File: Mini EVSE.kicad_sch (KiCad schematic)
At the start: 39 parts, among them IC1 ATtiny84-20P, IC2 UCC23511QDWYRQ1, IC3 TLP3547_TP1,F_O, J1 ICP, SW1 SW_DIP_x01, X1 15.36MHz

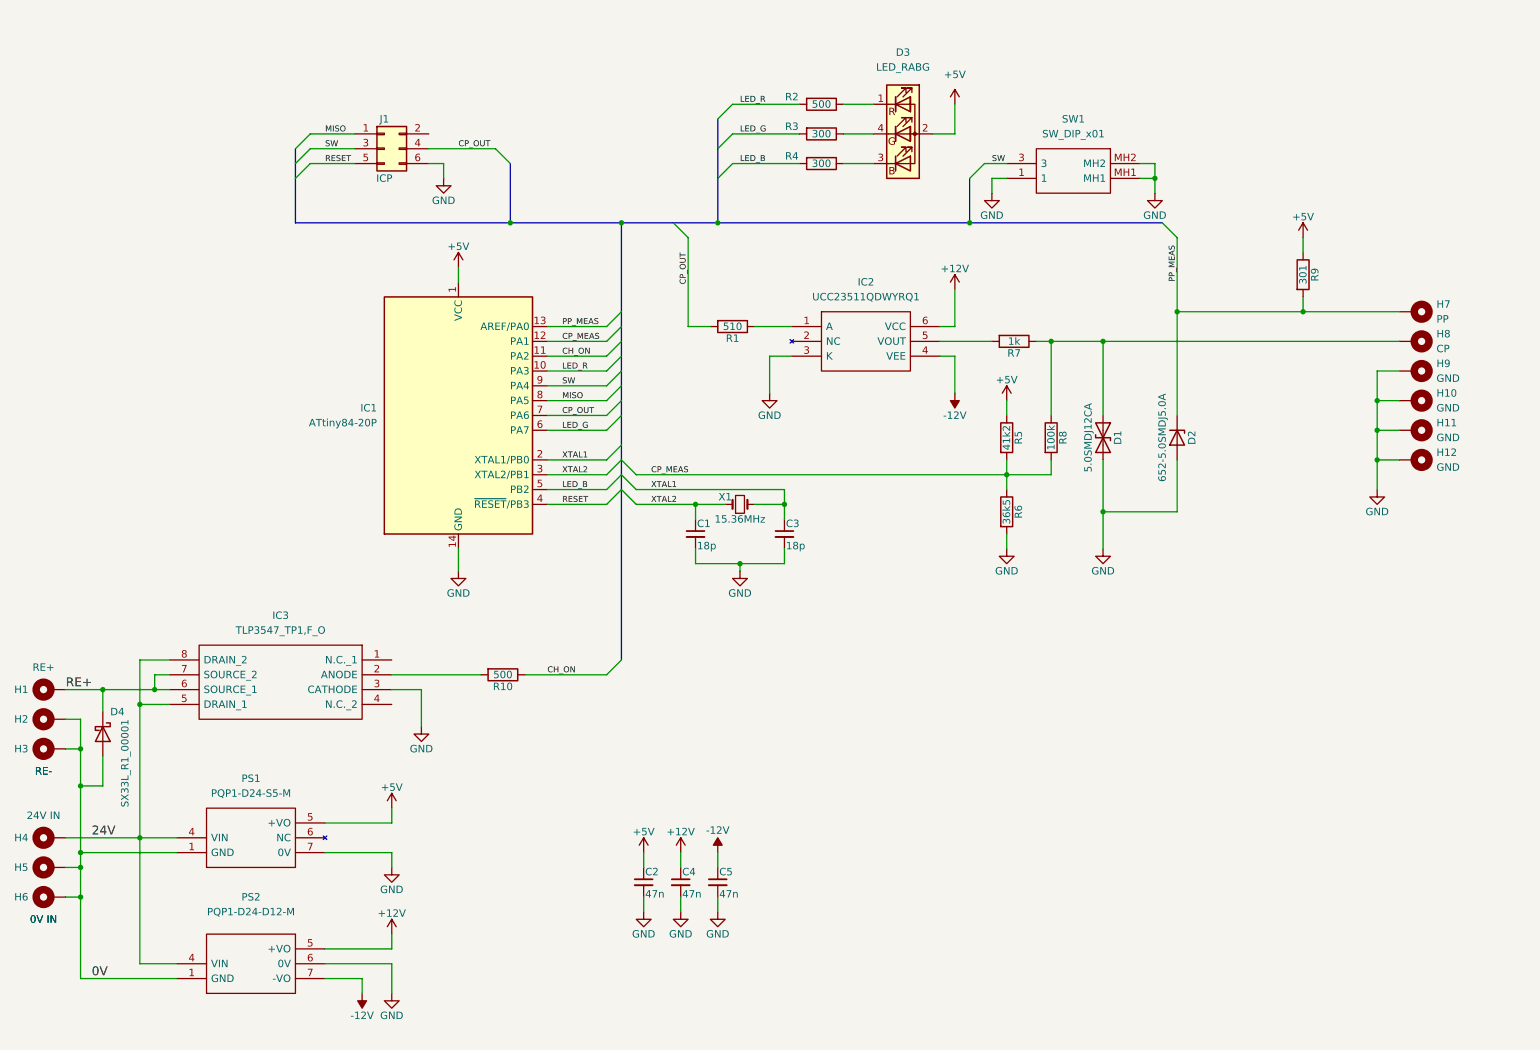
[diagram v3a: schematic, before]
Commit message: Working on better EMC immunity
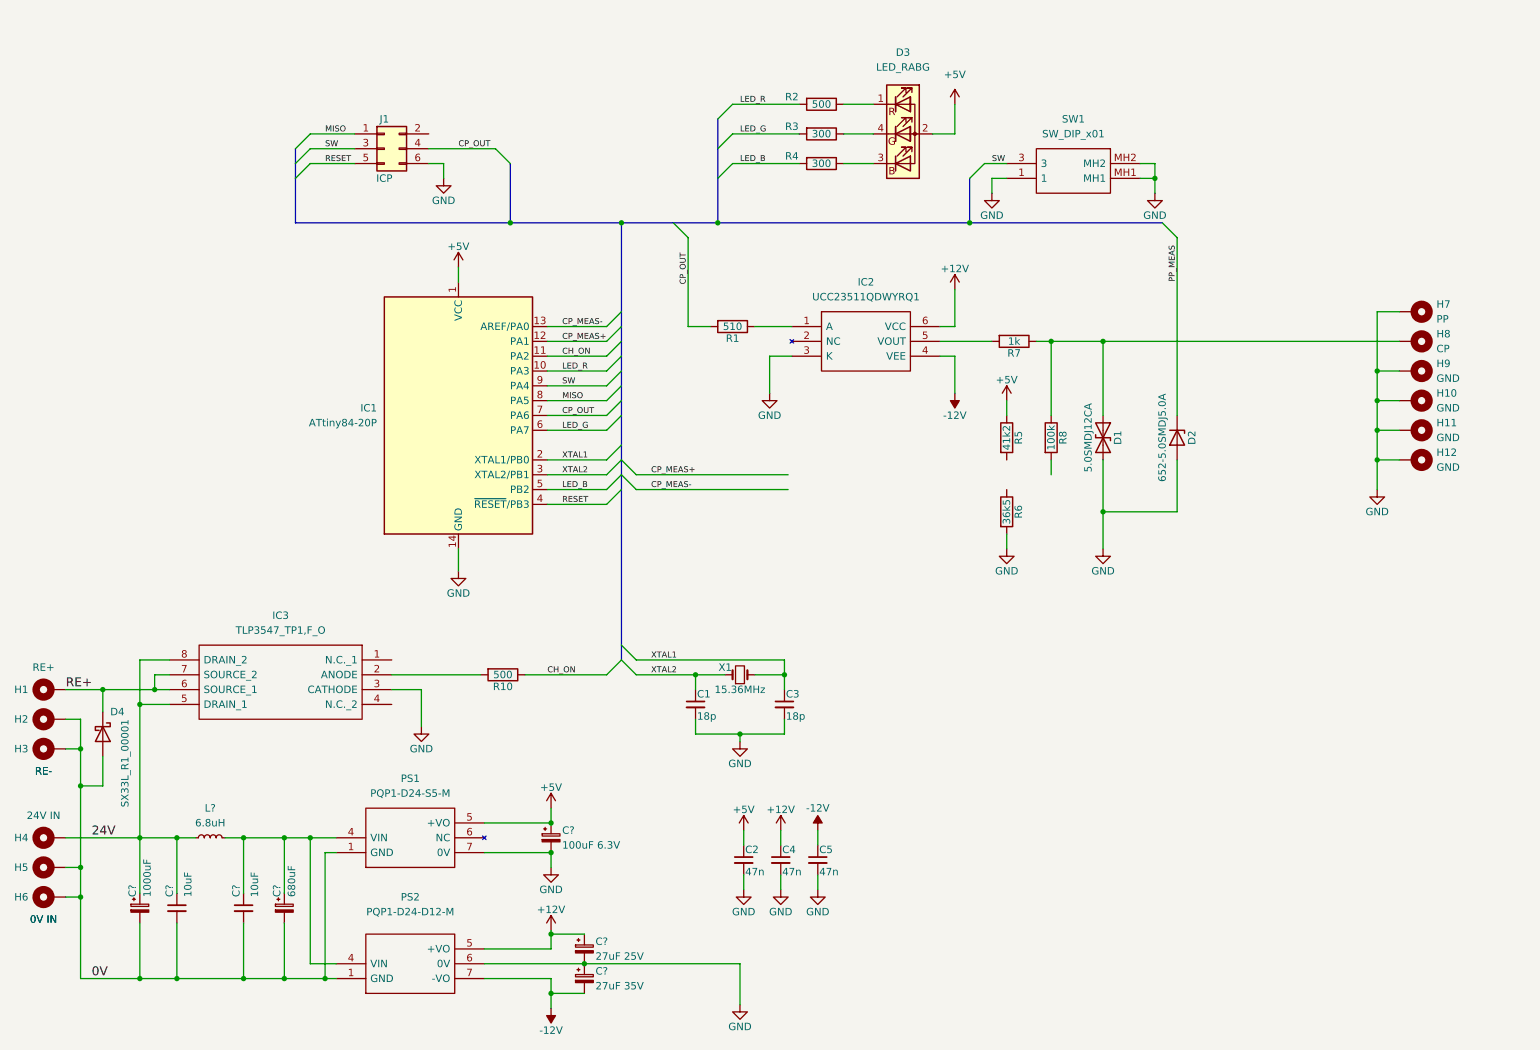
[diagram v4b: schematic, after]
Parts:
- removed R9: 301, Resistor_SMD:R_1210_3225Metric_Pad1.30x2.65mm_HandSolder, symbol Device:R
- added C? (x2): 10uF, symbol Device:C_Small
- added C?: 27uF 25V, symbol Device:C_Polarized_Small
- added C?: 1000uF, symbol Device:C_Polarized_Small
- added C?: 27uF 35V, symbol Device:C_Polarized_Small
- added C?: 100uF 6.3V, symbol Device:C_Polarized_Small
- added C?: 680uF, symbol Device:C_Polarized_Small
- added L?: 6.8uH, symbol Device:L_Small
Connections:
- net +12V: now also C?.1
- net +5V: now also C?.1
- net -12V: now also C?.2
- net 0V: now also C?.2, C?.2, C?.2, C?.2
- net 24V: now also C?.1, C?.1, L?.1; no longer PS1.4 (VIN), PS2.4 (VIN)
- net GND: now also H7.1, C?.1, C?.2, C?.2
- net PP_MEAS: no longer H7.1, IC1.13 (AREF/PA0)
- removed net CP_MEAS: IC1.12 (PA1), R5.2, R6.1, R8.2
- new net: C?.1, C?.1, L?.2, PS1.4 (VIN), PS2.4 (VIN)
- new net CP_MEAS+: IC1.12 (PA1)
- new net CP_MEAS-: IC1.13 (AREF/PA0)
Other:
- moved on the sheet: C1, C2, C3, C4, C5, PS1, PS2, X1

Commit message: Better EMC protection
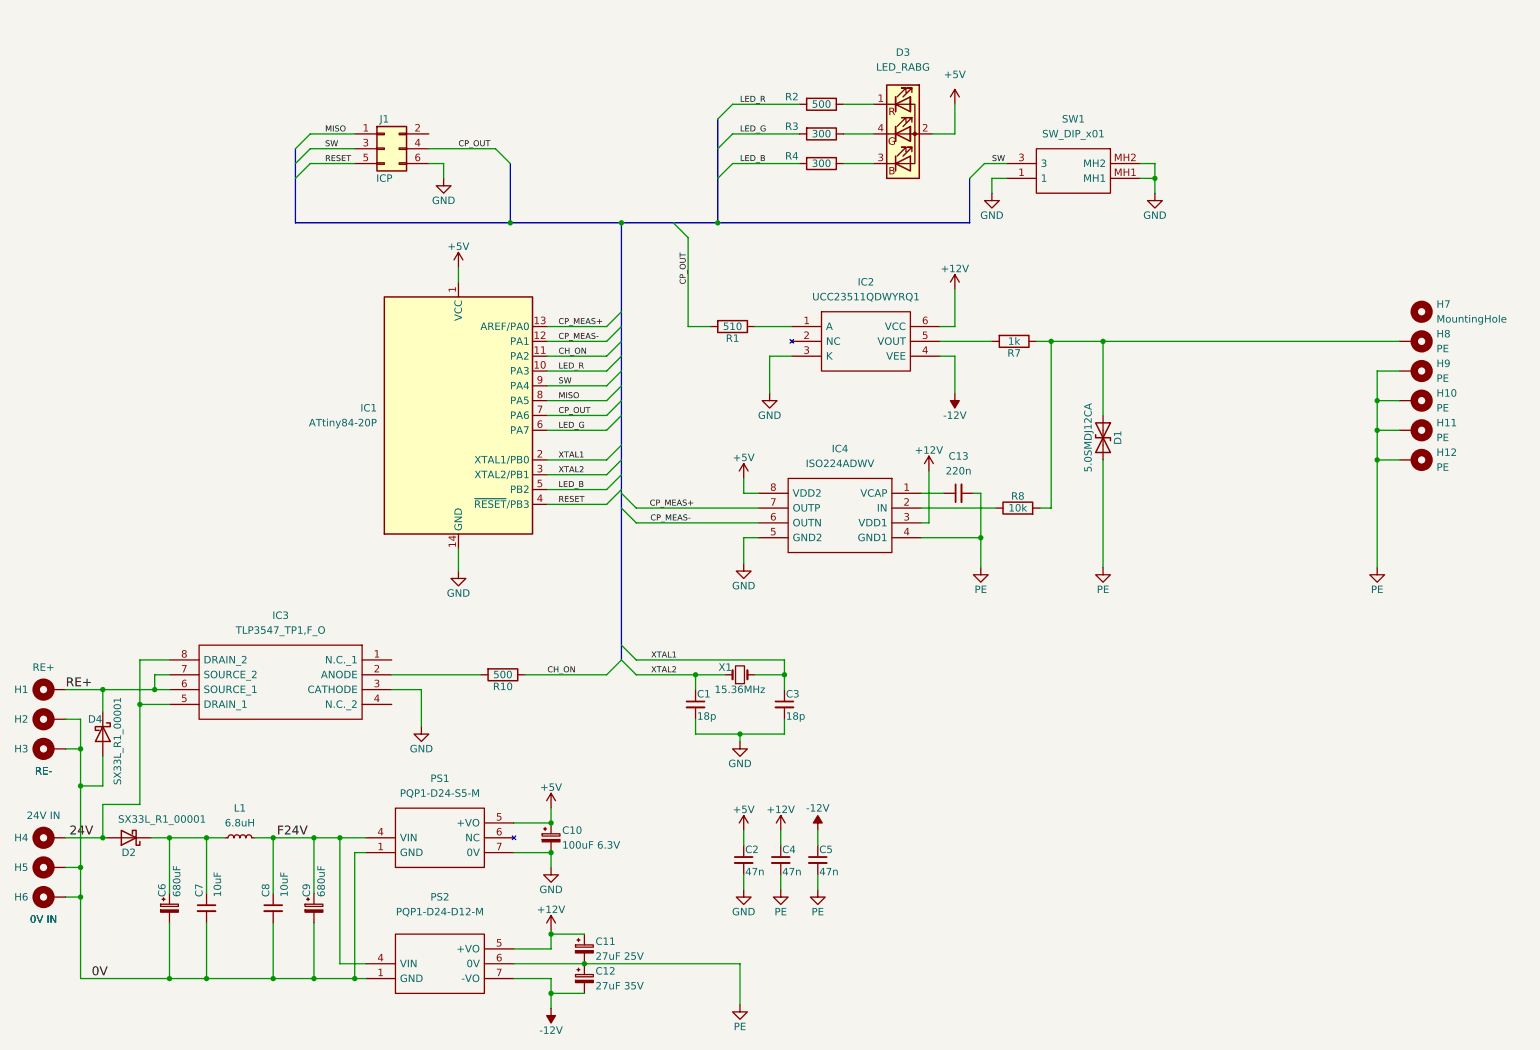
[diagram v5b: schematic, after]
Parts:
- removed D2: 652-5.0SMDJ5.0A, Diode_SMD:D_SMC, symbol Device:D_Zener
- removed H7: PP, TestPoint:TestPoint_Loop_D2.60mm_Drill1.4mm_Beaded, symbol Mechanical:MountingHole_Pad
- removed R5: 41k2, Resistor_SMD:R_1210_3225Metric_Pad1.30x2.65mm_HandSolder, symbol Device:R
- removed R6: 36k5, Resistor_SMD:R_1210_3225Metric_Pad1.30x2.65mm_HandSolder, symbol Device:R
- added C13: 220n, Capacitor_SMD:C_1206_3216Metric_Pad1.33x1.80mm_HandSolder, symbol Device:C_Small
- added D2: SX33L_R1_00001, Diode_SMD:D_SMA_Handsoldering, symbol Device:D_Schottky
- added H7: MountingHole, MountingHole:MountingHole_2.1mm, symbol Mechanical:MountingHole
- added IC4: ISO224ADWV, SamacSys_Parts:SOIC127P1150X280-8N, symbol SamacSys_Parts:ISO224ADWV
- C10: renamed from C?; footprint (none) -> Capacitor_SMD:CP_Elec_6.3x5.9
- C11, C12: renamed from C?; footprint (none) -> Capacitor_SMD:CP_Elec_5x5.8
- C6: renamed from C?; value 1000uF -> 680uF; footprint (none) -> Capacitor_SMD:CP_Elec_10x10.5
- C7, C8: renamed from C?; footprint (none) -> Capacitor_SMD:C_1206_3216Metric_Pad1.33x1.80mm_HandSolder
- C9: renamed from C?; footprint (none) -> Capacitor_SMD:CP_Elec_10x10.5
- H10, H11, H12, H9: value GND -> PE
- H8: value CP -> PE
- L1: renamed from L?; footprint (none) -> Inductor_SMD:L_1210_3225Metric_Pad1.42x2.65mm_HandSolder
- R1, R10, R2, R3, R4, R7: footprint Resistor_SMD:R_1210_3225Metric_Pad1.30x2.65mm_HandSolder -> Resistor_SMD:R_1206_3216Metric_Pad1.30x1.75mm_HandSolder
- R8: value 100k -> 10k; footprint Resistor_SMD:R_1210_3225Metric_Pad1.30x2.65mm_HandSolder -> Resistor_SMD:R_1206_3216Metric_Pad1.30x1.75mm_HandSolder
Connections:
- net +12V: now also IC4.3 (VDD1)
- net +5V: now also IC4.8 (VDD2)
- net 24V: now also D2.2 (A); no longer C6.1, C7.1, L1.1
- net CP_MEAS+: now also IC1.13 (AREF/PA0), IC4.7 (OUTP); no longer IC1.12 (PA1)
- net CP_MEAS-: now also IC1.12 (PA1), IC4.6 (OUTN); no longer IC1.13 (AREF/PA0)
- net GND: now also IC4.5 (GND2); no longer C11.2, C12.1, C4.2, C5.2, D1.2 (A2), H10.1, H11.1, H12.1, H9.1, PS2.6 (0V)
- net at D1.1 (A1), H8.1, R7.1: now also R8.2; no longer R8.1
- net F24V: now reaches C8.1, C9.1, L1.2, PS1.4 (VIN), PS2.4 (VIN)
- new net: IC4.2 (IN), R8.1
- new net: C6.1, C7.1, D2.1 (K), L1.1
- new net: C13.1, IC4.1 (VCAP)
- new net PE: C11.2, C12.1, C13.2, C4.2, C5.2, D1.2 (A2), H10.1, H11.1, H12.1, H9.1, IC4.4 (GND1), PS2.6 (0V)
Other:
- moved on the sheet: C6, C7, C8, C9, L1, PS1, PS2, R8

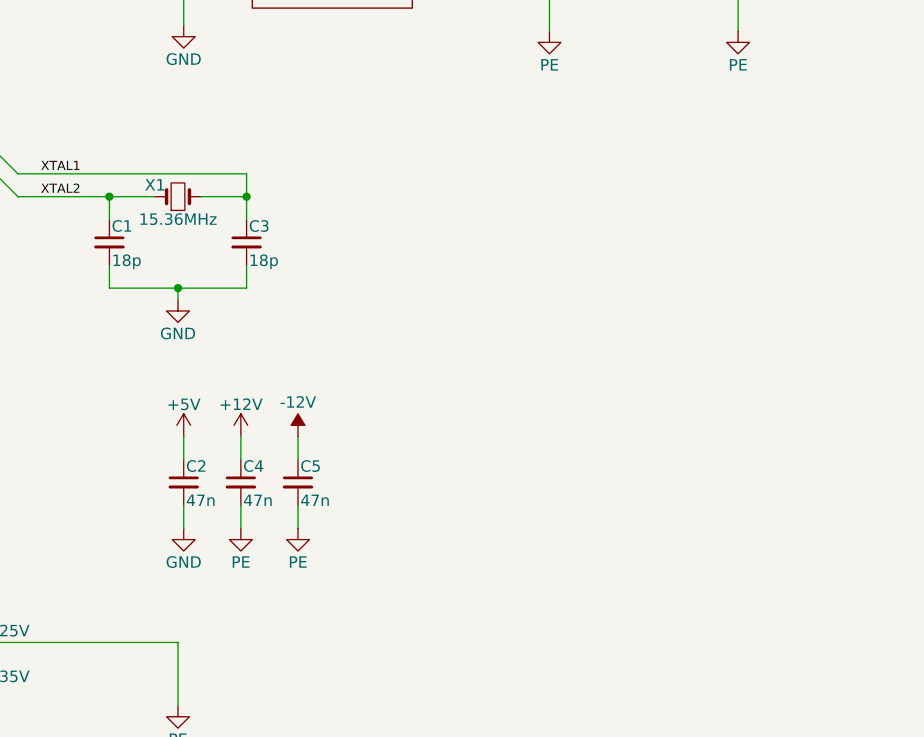
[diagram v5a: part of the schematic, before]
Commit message: More decoupling, layout adjustments
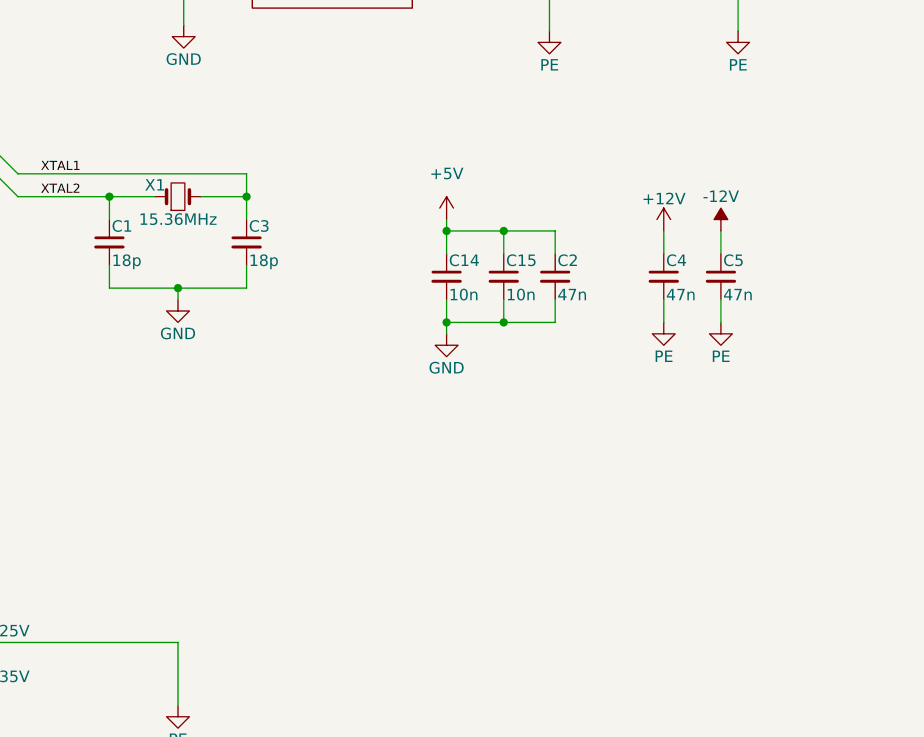
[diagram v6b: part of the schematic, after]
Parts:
- added C14, C15: 10n, Capacitor_SMD:C_1206_3216Metric_Pad1.33x1.80mm_HandSolder, symbol Device:C_Small
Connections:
- net +5V: now also C14.1, C15.1
- net GND: now also C14.2, C15.2
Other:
- moved on the sheet: C2, C4, C5

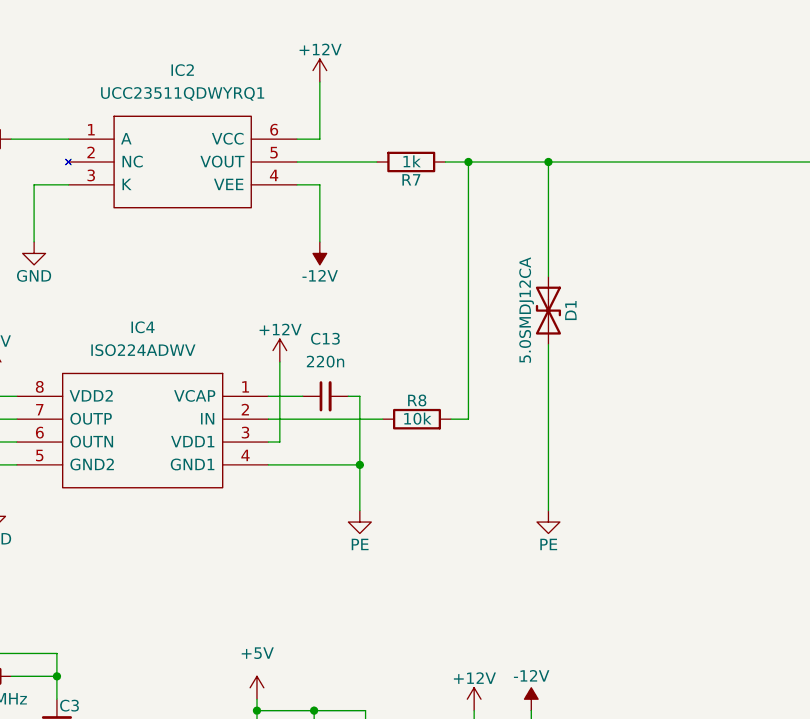
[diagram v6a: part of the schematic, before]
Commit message: Added possible input decoupling cap
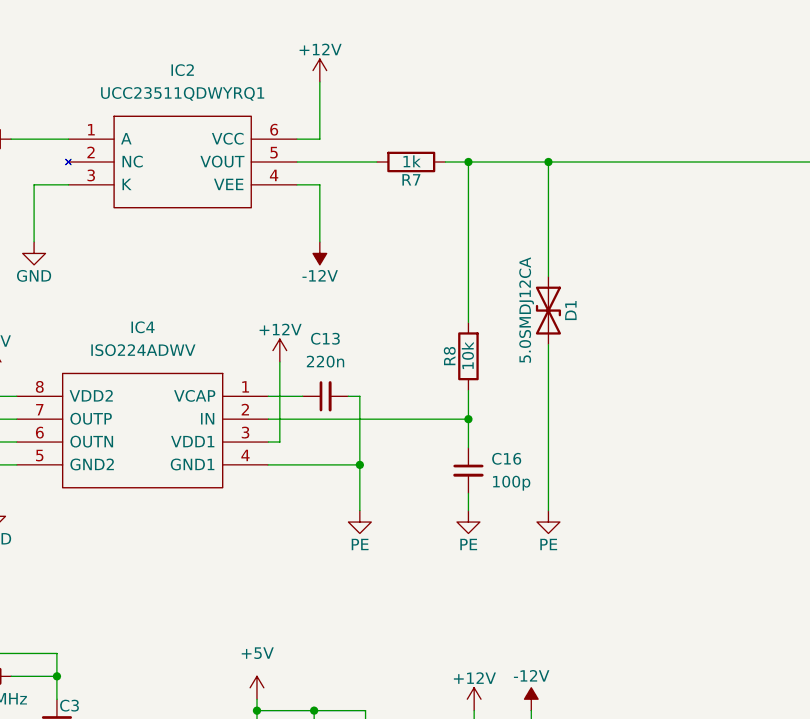
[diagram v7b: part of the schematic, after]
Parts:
- added C16: 100p, Capacitor_SMD:C_1206_3216Metric_Pad1.33x1.80mm_HandSolder, symbol Device:C_Small
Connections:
- net PE: now also C16.2
- net at IC4.2 (IN), R8.1: now also C16.1
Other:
- moved on the sheet: R8
